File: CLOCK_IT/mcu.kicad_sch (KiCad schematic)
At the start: 11 parts, among them IC1 APS6404L-3SQR-SN, U1 ESP32-S3R8, U2 W25Q128JVSIQ

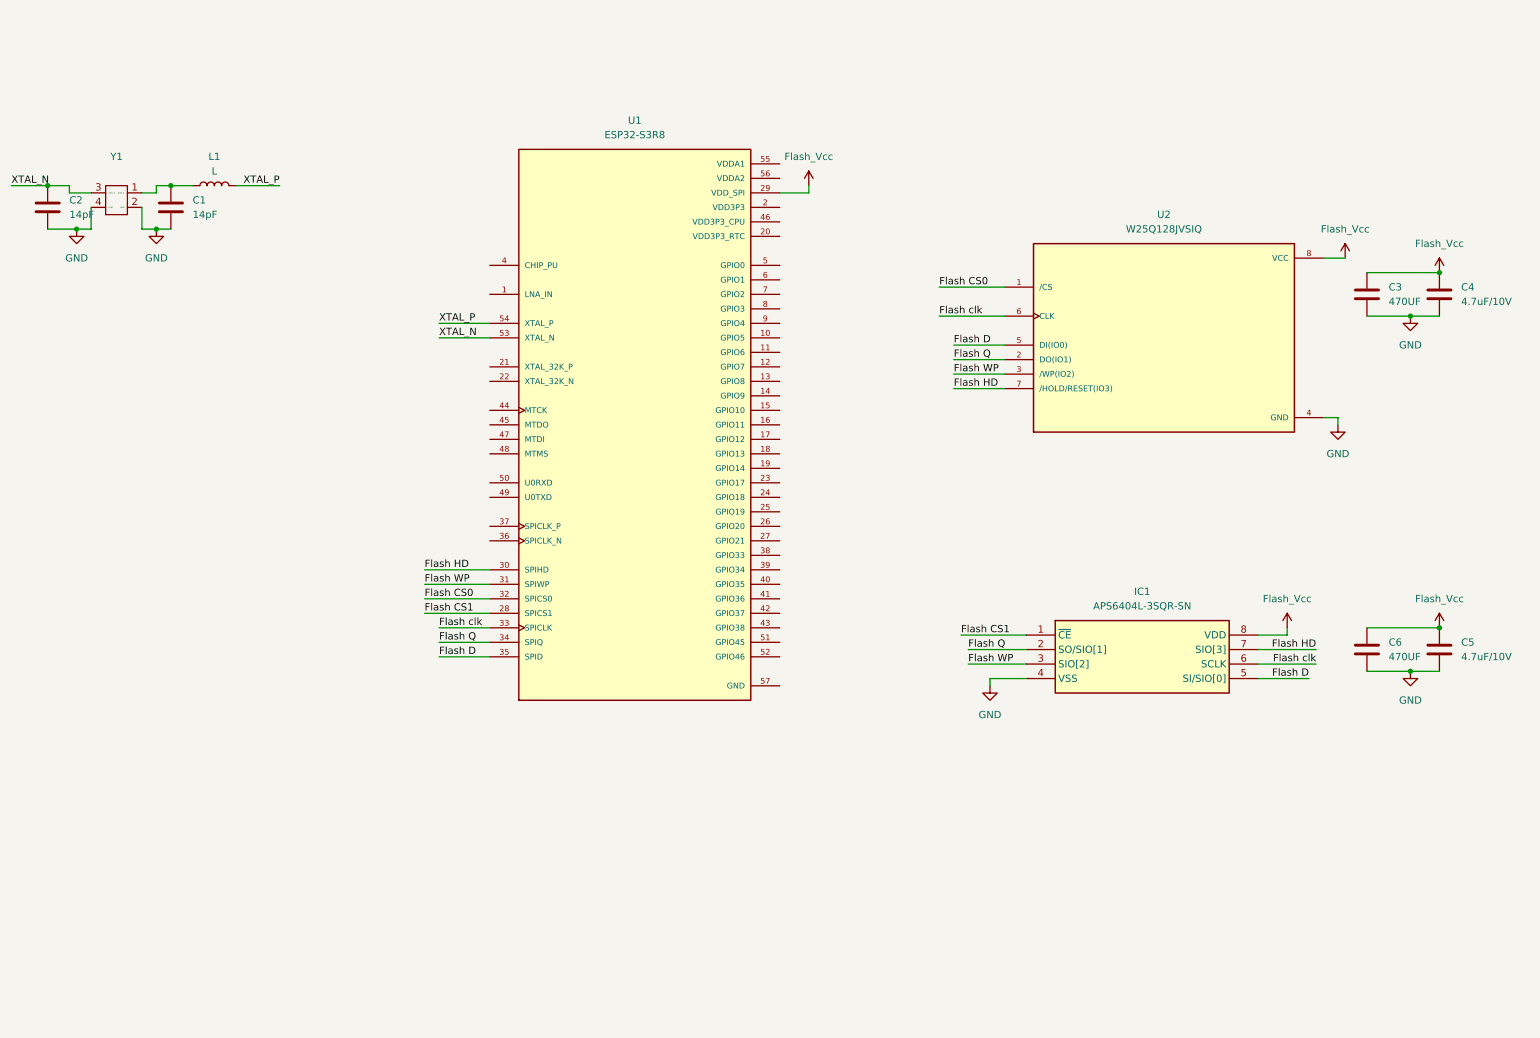
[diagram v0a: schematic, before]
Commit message: :memo:added SD CARD-TF-
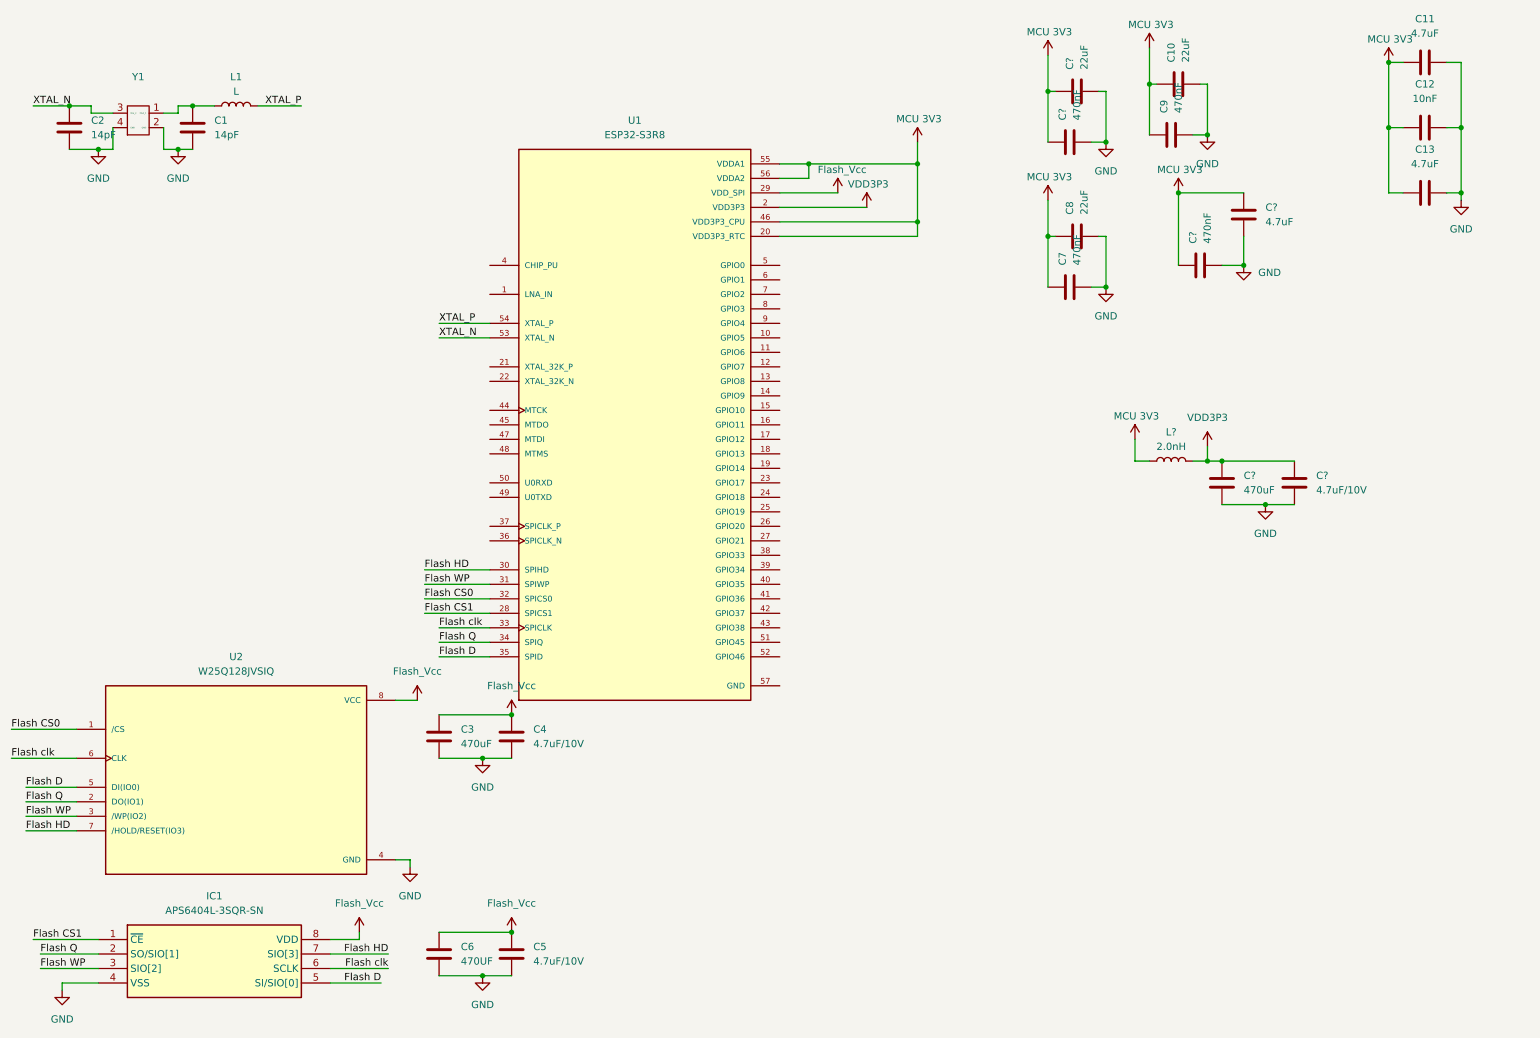
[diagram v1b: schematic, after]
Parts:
- added C10, C8, C?: 22uF, symbol Device:C
- added C11, C13, C?: 4.7uF, symbol Device:C
- added C12: 10nF, symbol Device:C
- added C7, C9, C? (x2): 470nF, symbol Device:C
- added C?: 470uF, symbol Device:C
- added C?: 4.7uF/10V, symbol Device:C
- added L?: 2.0nH, symbol Device:L
- C3: value 470UF -> 470uF
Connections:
- net GND: now also C10.2, C11.2, C12.2, C13.2, C7.2, C8.2, C9.2, C?.2, C?.2, C?.2, C?.2, C?.2, C?.2
- net VDD3P3: now also C?.1, C?.1, L?.2
- net MCU 3V3: now reaches U1.20 (VDD3P3_RTC)
- net MCU 3V3: now also U1.46 (VDD3P3_CPU), U1.55 (VDDA1), U1.56 (VDDA2), C10.1, C11.1, C12.1, C13.1, C7.1, C8.1, C9.1, C?.1, C?.1, C?.1, C?.1, L?.1
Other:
- moved on the sheet: C1, C2, C3, C4, C5, C6, IC1, L1, U2, Y1

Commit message: :tada: added camera pin an pinout naming
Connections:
- net SCL_I2C: now reaches U1.16 (GPIO11)
- net SDA_I2C: now reaches U1.17 (GPIO12)
- net SCL_I2S: now reaches U1.18 (GPIO13)
- net SDA_I2S: now reaches U1.19 (GPIO14)
- net USB_D-: now reaches U1.25 (GPIO19)
- net USB_D+: now reaches U1.26 (GPIO20)
- net SPI_MISO: now reaches U1.40 (GPIO35)
- net SPICLK: now reaches U1.41 (GPIO36)
- net SPI_MOSI: now reaches U1.42 (GPIO37)
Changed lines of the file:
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@@
+	(wire
+		(pts
+			(xy 152.4 92.71) (xy 163.83 92.71)
+		)
+		(stroke
+			(width 0)
+			(type default)
+		)
+	)
 	(wire
 		(pts
@@
 	(wire
 		(pts
+			(xy 152.4 115.57) (xy 162.56 115.57)
+		)
+		(stroke
+			(width 0)
+			(type default)
+		)
+	)
+	(wire
+		(pts
 			(xy 269.24 21.59) (xy 271.78 21.59)
 		)
@@
 	(wire
 		(pts
+			(xy 152.4 100.33) (xy 162.56 100.33)
+		)
+		(stroke
+			(width 0)
+			(type default)
+		)
+	)
+	(wire
+		(pts
 			(xy 199.39 52.07) (xy 200.66 52.07)
 		)
@@
 	(wire
 		(pts
+			(xy 152.4 87.63) (xy 163.83 87.63)
+		)
+		(stroke
+			(width 0)
+			(type default)
+		)
+	)
+	(wire
+		(pts
 			(xy 271.78 33.02) (xy 271.78 44.45)
 		)
@@
 	(wire
 		(pts
+			(xy 152.4 118.11) (xy 162.56 118.11)
+		)
+		(stroke
+			(width 0)
+			(type default)
+		)
+	)
+	(wire
+		(pts
 			(xy 92.71 123.19) (xy 101.6 123.19)
 		)
@@
 	(wire
 		(pts
+			(xy 152.4 113.03) (xy 162.56 113.03)
+		)
+		(stroke
+			(width 0)
+			(type default)
+		)
+	)
+	(wire
+		(pts
 			(xy 199.39 26.67) (xy 199.39 35.56)
 		)
@@
 	(wire
 		(pts
+			(xy 152.4 90.17) (xy 163.83 90.17)
+		)
+		(stroke
+			(width 0)
+			(type default)
+		)
+	)
+	(wire
+		(pts
 			(xy 152.4 46.99) (xy 167.64 46.99)
 		)
@@
 	(wire
 		(pts
+			(xy 152.4 85.09) (xy 163.83 85.09)
+		)
+		(stroke
+			(width 0)
+			(type default)
+		)
+	)
+	(wire
+		(pts
 			(xy 271.78 21.59) (xy 271.78 33.02)
 		)
@@
 		(pts
 			(xy 73.66 182.88) (xy 82.55 182.88)
+		)
+		(stroke
+			(width 0)
+			(type default)
+		)
+	)
+	(wire
+		(pts
+			(xy 152.4 102.87) (xy 162.56 102.87)
 		)
 		(stroke
@@
 		)
 	)
+	(label "SPI_MISO"
+		(at 162.56 113.03 180)
+		(effects
+			(font
+				(size 1.27 1.27)
+			)
+			(justify right bottom)
+		)
+	)
 	(label "Flash D"
 		(at 92.71 125.73 0)
@@
 		)
 	)
+	(label "SPICLK"
+		(at 162.56 115.57 180)
+		(effects
+			(font
+				(size 1.27 1.27)
+			)
+			(justify right bottom)
+		)
+	)
+	(label "USB_D+"
+		(at 162.56 102.87 180)
+		(effects
+			(font
+				(size 1.27 1.27)
+			)
+			(justify right bottom)
+		)
+	)
 	(label "XTAL_N"
 		(at 21.59 29.21 0)
@@
 		)
 	)
+	(label "USB_D-"
+		(at 162.56 100.33 180)
+		(effects
+			(font
+				(size 1.27 1.27)
+			)
+			(justify right bottom)
+		)
+	)
 	(label "Flash CS0"
 		(at 90.17 115.57 0)
@@
 		)
 	)
+	(label "SPI_MOSI"
+		(at 162.56 118.11 180)
+		(effects
+			(font
+				(size 1.27 1.27)
+			)
+			(justify right bottom)
+		)
+	)
 	(label "Flash clk"
 		(at 17.78 143.51 0)
@@
 		)
 	)
+	(label "SCL_I2C"
+		(at 163.83 85.09 180)
+		(effects
+			(font
+				(size 1.27 1.27)
+			)
+			(justify right bottom)
+		)
+	)
+	(label "SCL_I2S"
+		(at 163.83 90.17 180)
+		(effects
+			(font
+				(size 1.27 1.27)
+			)
+			(justify right bottom)
+		)
+	)
 	(label "Flash HD"
 		(at 20.32 156.21 0)
@@
 		)
 	)
+	(label "SDA_I2C"
+		(at 163.83 87.63 180)
+		(effects
+			(font
+				(size 1.27 1.27)
+			)
+			(justify right bottom)
+		)
+	)
 	(label "Flash WP"
 		(at 90.17 113.03 0)
@@
 		(effects
 			(font
+				(size 1.27 1.27)
+			)
+			(justify right bottom)
+		)
+	)
+	(label "SDA_I2S"
+		(at 163.83 92.71 180)
+		(effects
+			(font
